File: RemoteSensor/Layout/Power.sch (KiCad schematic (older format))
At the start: 22 parts, among them J1 USB_B_Micro, J2 BATT_CONN, Q1 2N7002, U1 MCP73831-2-OT, U2 LM3670MF, U3 BD48ExxG, U4 BD48ExxG, U5 LM3670MF

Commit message: Add an IO expander
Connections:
- wire segments 73 -> 75
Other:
- moved on the sheet: R5
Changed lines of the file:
@@
 L SparkFun-PowerSymbols:GND #GND0101
 U 1 1 5EEB1274
-P 9650 5000
-F 0 "#GND0101" H 9700 4950 45  0001 L BNN
-F 1 "GND" H 9650 4830 45  0000 C CNN
-F 2 "" H 9650 4900 60  0001 C CNN
-F 3 "" H 9650 4900 60  0001 C CNN
-	1    9650 5000
+P 9650 5200
+F 0 "#GND0101" H 9700 5150 45  0001 L BNN
+F 1 "GND" H 9650 5030 45  0000 C CNN
+F 2 "" H 9650 5100 60  0001 C CNN
+F 3 "" H 9650 5100 60  0001 C CNN
+	1    9650 5200
 	1    0    0    -1
 $EndComp
@@
 	8950 4150 9350 4150
 $Comp
-L dk_Transistors-FETs-MOSFETs-Single:2N7002 Q1
-U 1 1 5EEB1294
-P 8950 4800
-F 0 "Q1" H 9058 4853 60  0000 L CNN
-F 1 "2N7002" H 9058 4747 60  0000 L CNN
-F 2 "digikey-footprints:SOT-23-3" H 9150 5000 60  0001 L CNN
-F 3 "https://www.onsemi.com/pub/Collateral/NDS7002A-D.PDF" H 9150 5100 60  0001 L CNN
-F 4 "2N7002NCT-ND" H 9150 5200 60  0001 L CNN "Digi-Key_PN"
-F 5 "2N7002" H 9150 5300 60  0001 L CNN "MPN"
-F 6 "Discrete Semiconductor Products" H 9150 5400 60  0001 L CNN "Category"
-F 7 "Transistors - FETs, MOSFETs - Single" H 9150 5500 60  0001 L CNN "Family"
-F 8 "https://www.onsemi.com/pub/Collateral/NDS7002A-D.PDF" H 9150 5600 60  0001 L CNN "DK_Datasheet_Link"
-F 9 "/product-detail/en/on-semiconductor/2N7002/2N7002NCT-ND/244664" H 9150 5700 60  0001 L CNN "DK_Detail_Page"
-F 10 "MOSFET N-CH 60V 115MA SOT-23" H 9150 5800 60  0001 L CNN "Description"
-F 11 "ON Semiconductor" H 9150 5900 60  0001 L CNN "Manufacturer"
-F 12 "Active" H 9150 6000 60  0001 L CNN "Status"
-	1    8950 4800
-	1    0    0    1
-$EndComp
-$Comp
 L Regulator_Switching:LM3670MF U5
 U 1 1 5EEB129A
@@
 	1    0    0    -1
 $EndComp
-Wire Wire Line
-	8950 4600 8950 4450
-Connection ~ 8950 4450
 $Comp
 L Device:R_US R5
 U 1 1 5EEB12A2
-P 8450 4850
-F 0 "R5" H 8518 4896 50  0000 L CNN
-F 1 "10k" H 8518 4805 50  0000 L CNN
-F 2 "Resistor_SMD:R_0603_1608Metric_Pad1.05x0.95mm_HandSolder" V 8490 4840 50  0001 C CNN
-F 3 "~" H 8450 4850 50  0001 C CNN
-	1    8450 4850
-	1    0    0    -1
-$EndComp
-Wire Wire Line
-	8450 4700 8650 4700
-Wire Wire Line
-	8450 5000 8950 5000
-Wire Wire Line
-	8950 5000 9650 5000
-Wire Wire Line
-	9650 5000 9650 4550
-Connection ~ 8950 5000
-Connection ~ 9650 5000
+P 8650 5000
+F 0 "R5" H 8718 5046 50  0000 L CNN
+F 1 "10k" H 8718 4955 50  0000 L CNN
+F 2 "Resistor_SMD:R_0603_1608Metric_Pad1.05x0.95mm_HandSolder" V 8690 4990 50  0001 C CNN
+F 3 "~" H 8650 5000 50  0001 C CNN
+	1    8650 5000
+	1    0    0    -1
+$EndComp
 Wire Wire Line
 	8950 4150 8000 4150
 Connection ~ 8950 4150
 Connection ~ 8000 4150
-Wire Wire Line
-	8000 5000 8450 5000
-Wire Wire Line
-	8000 4450 8000 5000
-Connection ~ 8450 5000
 $Comp
 L SparkFun-PowerSymbols:V_USB #SUPPLY0102
 U 1 1 5EEB12BC
-P 8450 4100
-F 0 "#SUPPLY0102" H 8500 4100 45  0001 L BNN
-F 1 "V_USB" H 8450 4376 45  0000 C CNN
-F 2 "XXX-00000" H 8450 4281 60  0000 C CNN
-F 3 "" H 8450 4100 60  0001 C CNN
-	1    8450 4100
-	1    0    0    -1
-$EndComp
-Wire Wire Line
-	8450 4100 8450 4700
-Connection ~ 8450 4700
+P 8650 4000
+F 0 "#SUPPLY0102" H 8700 4000 45  0001 L BNN
+F 1 "V_USB" H 8650 4276 45  0000 C CNN
+F 2 "XXX-00000" H 8650 4181 60  0000 C CNN
+F 3 "" H 8650 4000 60  0001 C CNN
+	1    8650 4000
+	1    0    0    -1
+$EndComp
 $Comp
 L Connector:USB_B_Micro J?
@@
 	7150 2100 7500 2100
 Connection ~ 7150 2100
+$Comp
+L dk_Transistors-FETs-MOSFETs-Single:2N7002 Q1
+U 1 1 5EEB1294
+P 8950 4700
+F 0 "Q1" H 9058 4753 60  0000 L CNN
+F 1 "2N7002" H 9058 4647 60  0000 L CNN
+F 2 "digikey-footprints:SOT-23-3" H 9150 4900 60  0001 L CNN
+F 3 "https://www.onsemi.com/pub/Collateral/NDS7002A-D.PDF" H 9150 5000 60  0001 L CNN
+F 4 "2N7002NCT-ND" H 9150 5100 60  0001 L CNN "Digi-Key_PN"
+F 5 "2N7002" H 9150 5200 60  0001 L CNN "MPN"
+F 6 "Discrete Semiconductor Products" H 9150 5300 60  0001 L CNN "Category"
+F 7 "Transistors - FETs, MOSFETs - Single" H 9150 5400 60  0001 L CNN "Family"
+F 8 "https://www.onsemi.com/pub/Collateral/NDS7002A-D.PDF" H 9150 5500 60  0001 L CNN "DK_Datasheet_Link"
+F 9 "/product-detail/en/on-semiconductor/2N7002/2N7002NCT-ND/244664" H 9150 5600 60  0001 L CNN "DK_Detail_Page"
+F 10 "MOSFET N-CH 60V 115MA SOT-23" H 9150 5700 60  0001 L CNN "Description"
+F 11 "ON Semiconductor" H 9150 5800 60  0001 L CNN "Manufacturer"
+F 12 "Active" H 9150 5900 60  0001 L CNN "Status"
+	1    8950 4700
+	1    0    0    -1
+$EndComp
+Wire Wire Line
+	8950 4500 8950 4450
+Connection ~ 8950 4450
+Wire Wire Line
+	8650 4800 8650 4850
+Wire Wire Line
+	8650 5150 8650 5200
+Wire Wire Line
+	8650 5200 8950 5200
+Wire Wire Line
+	8950 5200 8950 4900
+Wire Wire Line
+	8000 4450 8000 5200
+Wire Wire Line
+	8000 5200 8650 5200
+Connection ~ 8650 5200
+Wire Wire Line
+	8950 5200 9650 5200
+Connection ~ 8950 5200
+Wire Wire Line
+	9650 5200 9650 4550
+Connection ~ 9650 5200
+Wire Wire Line
+	8650 4000 8650 4800
+Connection ~ 8650 4800
 $EndSCHEMATC

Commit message: Assign footprints
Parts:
- L1: footprint Inductor_SMD:L_0603_1608Metric_Pad1.05x0.95mm_HandSolder -> Inductor_SMD:L_Taiyo-Yuden_NR-24xx_HandSoldering
- U5: value LM3670MF -> LM3671MF
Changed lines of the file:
@@
 	8950 4150 9350 4150
-$Comp
-L Regulator_Switching:LM3670MF U5
-U 1 1 5EEB129A
-P 9650 4250
-F 0 "U5" H 9650 4575 50  0000 C CNN
-F 1 "LM3670MF" H 9650 4484 50  0000 C CNN
-F 2 "Package_TO_SOT_SMD:TSOT-23-5" H 9700 4000 50  0001 L CNN
-F 3 "http://www.ti.com/lit/ds/symlink/lm3670.pdf" H 9400 3900 50  0001 C CNN
-	1    9650 4250
-	1    0    0    -1
-$EndComp
 $Comp
 L Device:R_US R5
@@
 F 0 "L1" V 3190 6300 50  0000 C CNN
 F 1 "2.2u" V 3099 6300 50  0000 C CNN
-F 2 "Inductor_SMD:L_0603_1608Metric_Pad1.05x0.95mm_HandSolder" H 3000 6300 50  0001 C CNN
+F 2 "Inductor_SMD:L_Taiyo-Yuden_NR-24xx_HandSoldering" H 3000 6300 50  0001 C CNN
 F 3 "~" H 3000 6300 50  0001 C CNN
 	1    3000 6300
@@
 	8650 4000 8650 4800
 Connection ~ 8650 4800
+$Comp
+L Regulator_Switching:LM3670MF U5
+U 1 1 5EEB129A
+P 9650 4250
+F 0 "U5" H 9650 4575 50  0000 C CNN
+F 1 "LM3671MF" H 9650 4484 50  0000 C CNN
+F 2 "Package_TO_SOT_SMD:TSOT-23-5" H 9700 4000 50  0001 L CNN
+F 3 "http://www.ti.com/lit/ds/symlink/lm3671.pdf" H 9400 3900 50  0001 C CNN
+	1    9650 4250
+	1    0    0    -1
+$EndComp
 $EndSCHEMATC

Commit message: Update sensor schematic
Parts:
- Q1: symbol dk_Transistors-FETs-MOSFETs-Single:2N7002 -> RemoteSensor-rescue:2N7002-dk_Transistors-FETs-MOSFETs-Single
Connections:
- net labels added: USBDM, USBDP
- wire segments 75 -> 79
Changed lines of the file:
@@
 EESchema Schematic File Version 4
-LIBS:RemoteSensor-cache
-EELAYER 29 0
+EELAYER 30 0
 EELAYER END
 $Descr A4 11693 8268
@@
 $EndDescr
 $Comp
-L SparkFun-PowerSymbols:V_BATT #SUPPLY0101
+L RemoteSensor-rescue:V_BATT-SparkFun-PowerSymbols #SUPPLY0101
 U 1 1 5EEB1246
 P 8000 4000
@@
 	8000 4000 8000 4150
 $Comp
-L SparkFun-PowerSymbols:GND #GND0101
+L RemoteSensor-rescue:GND-SparkFun-PowerSymbols #GND0101
 U 1 1 5EEB1274
 P 9650 5200
@@
 Connection ~ 8000 4150
 $Comp
-L SparkFun-PowerSymbols:V_USB #SUPPLY0102
+L RemoteSensor-rescue:V_USB-SparkFun-PowerSymbols #SUPPLY0102
 U 1 1 5EEB12BC
 P 8650 4000
@@
 $EndComp
 $Comp
-L SparkFun-PowerSymbols:V_USB #SUPPLY?
+L RemoteSensor-rescue:V_USB-SparkFun-PowerSymbols #SUPPLY?
 U 1 1 5EEC20CA
 P 2650 1600
@@
 $EndComp
 $Comp
-L SparkFun-PowerSymbols:GND #GND?
+L RemoteSensor-rescue:GND-SparkFun-PowerSymbols #GND?
 U 1 1 5EEC20D0
 P 1550 2650
@@
 $EndComp
 $Comp
-L SparkFun-PowerSymbols:V_USB #SUPPLY?
+L RemoteSensor-rescue:V_USB-SparkFun-PowerSymbols #SUPPLY?
 U 1 1 5EEC20F7
 P 2050 3700
@@
 $EndComp
 $Comp
-L SparkFun-PowerSymbols:V_BATT #SUPPLY?
+L RemoteSensor-rescue:V_BATT-SparkFun-PowerSymbols #SUPPLY?
 U 1 1 5EEC20FD
 P 2750 3700
@@
 	1450 5100 1450 4900
 $Comp
-L SparkFun-PowerSymbols:GND #GND?
+L RemoteSensor-rescue:GND-SparkFun-PowerSymbols #GND?
 U 1 1 5EEC2111
 P 2050 5100
@@
 $EndComp
 $Comp
-L SparkFun-PowerSymbols:GND #GND?
+L RemoteSensor-rescue:GND-SparkFun-PowerSymbols #GND?
 U 1 1 5EEC211E
 P 4900 4650
@@
 	2950 4400 2950 4300
 $Comp
-L SparkFun-PowerSymbols:3.3V #SUPPLY?
+L RemoteSensor-rescue:3.3V-SparkFun-PowerSymbols #SUPPLY?
 U 1 1 5EEC212C
 P 2950 4000
@@
 	1450 2500 1550 2500
 $Comp
-L SparkFun-PowerSymbols:V_BATT #SUPPLY?
+L RemoteSensor-rescue:V_BATT-SparkFun-PowerSymbols #SUPPLY?
 U 1 1 5EEC2137
 P 4900 4200
@@
 	3900 6700 3900 6600
 $Comp
-L SparkFun-PowerSymbols:3.3V #SUPPLY?
+L RemoteSensor-rescue:3.3V-SparkFun-PowerSymbols #SUPPLY?
 U 1 1 5EEC2172
 P 4350 6150
@@
 Connection ~ 3900 6300
 $Comp
-L SparkFun-PowerSymbols:GND #GND?
+L RemoteSensor-rescue:GND-SparkFun-PowerSymbols #GND?
 U 1 1 5EEC217B
 P 4500 2550
@@
 Connection ~ 4350 6300
 $Comp
-L SparkFun-PowerSymbols:V_USB #SUPPLY?
+L RemoteSensor-rescue:V_USB-SparkFun-PowerSymbols #SUPPLY?
 U 1 1 5EEC218D
 P 3900 1850
@@
 $EndComp
 $Comp
-L SparkFun-PowerSymbols:GND #GND?
+L RemoteSensor-rescue:GND-SparkFun-PowerSymbols #GND?
 U 1 1 5EF05E4C
 P 6050 4850
@@
 $EndComp
 $Comp
-L SparkFun-PowerSymbols:GND #GND?
+L RemoteSensor-rescue:GND-SparkFun-PowerSymbols #GND?
 U 1 1 5EF05E64
 P 6500 2550
@@
 	7150 2100 6900 2100
 $Comp
-L SparkFun-PowerSymbols:3.3V #SUPPLY?
+L RemoteSensor-rescue:3.3V-SparkFun-PowerSymbols #SUPPLY?
 U 1 1 5EF05E76
 P 7150 1700
@@
 $EndComp
 $Comp
-L SparkFun-PowerSymbols:3.3V #SUPPLY?
+L RemoteSensor-rescue:3.3V-SparkFun-PowerSymbols #SUPPLY?
 U 1 1 5EF05E7C
 P 6700 4000
@@
 $EndComp
 $Comp
-L SparkFun-PowerSymbols:V_USB #SUPPLY?
+L RemoteSensor-rescue:V_USB-SparkFun-PowerSymbols #SUPPLY?
 U 1 1 5EF05E82
 P 6500 1600
@@
 $EndComp
 $Comp
-L SparkFun-PowerSymbols:V_BATT #SUPPLY?
+L RemoteSensor-rescue:V_BATT-SparkFun-PowerSymbols #SUPPLY?
 U 1 1 5EF05E88
 P 6050 3900
@@
 	6500 1600 6500 1800
 $Comp
-L SparkFun-PowerSymbols:GND #GND0108
+L RemoteSensor-rescue:GND-SparkFun-PowerSymbols #GND0108
 U 1 1 5EF27A6F
 P 3900 6700
@@
 Connection ~ 7150 2100
 $Comp
-L dk_Transistors-FETs-MOSFETs-Single:2N7002 Q1
+L RemoteSensor-rescue:2N7002-dk_Transistors-FETs-MOSFETs-Single Q1
 U 1 1 5EEB1294
 P 8950 4700
@@
 	1    0    0    -1
 $EndComp
+Wire Wire Line
+	1850 2000 2050 2000
+Wire Wire Line
+	2050 2000 2050 2750
+Wire Wire Line
+	1850 2100 1950 2100
+Wire Wire Line
+	1950 2100 1950 2750
+Text GLabel 2050 2750 3    50   Input ~ 0
+USBDP
+Text GLabel 1950 2750 3    50   Input ~ 0
+USBDM
 $EndSCHEMATC

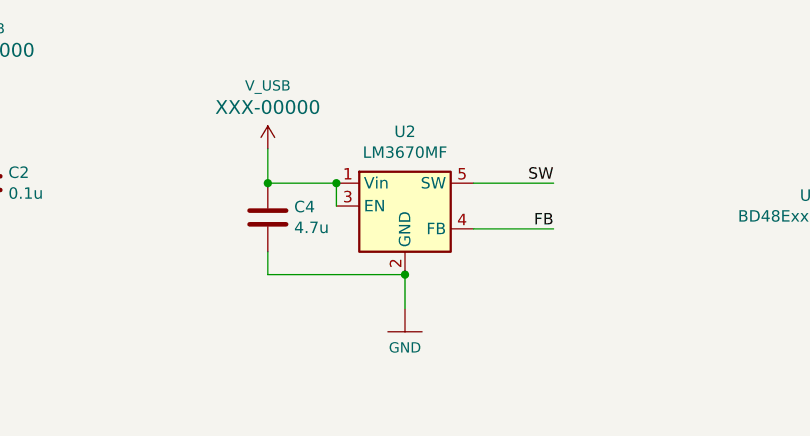
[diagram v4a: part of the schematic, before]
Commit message: Add footprints and component values
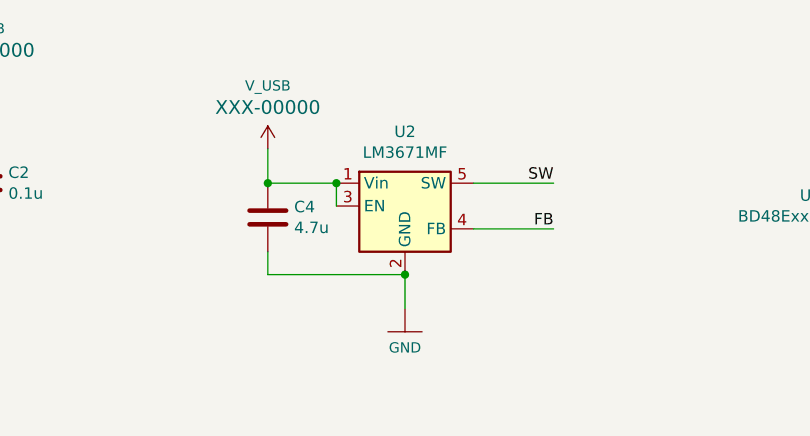
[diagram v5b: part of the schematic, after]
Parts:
- U2: value LM3670MF -> LM3671MF
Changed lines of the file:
@@
 AR Path="/5EE9FD3C/5EEC2141" Ref="U2"  Part="1"
 F 0 "U2" H 4500 2425 50  0000 C CNN
-F 1 "LM3670MF" H 4500 2334 50  0000 C CNN
+F 1 "LM3671MF" H 4500 2334 50  0000 C CNN
 F 2 "Package_TO_SOT_SMD:TSOT-23-5" H 4550 1850 50  0001 L CNN
 F 3 "http://www.ti.com/lit/ds/symlink/lm3670.pdf" H 4250 1750 50  0001 C CNN
